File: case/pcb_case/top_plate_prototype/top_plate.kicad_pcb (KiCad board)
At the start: 2 copper layers, 143.4 x 111.8 mm, 7 parts

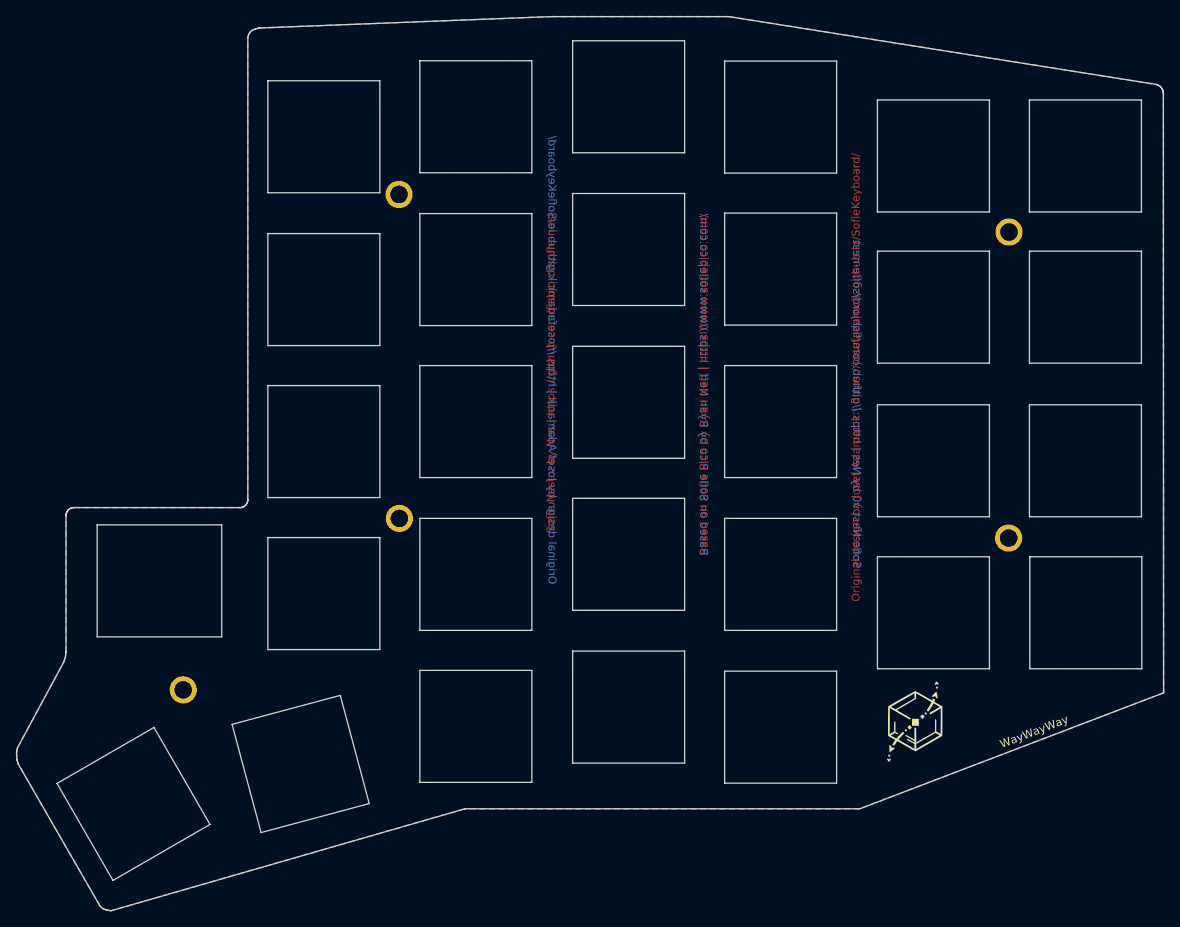
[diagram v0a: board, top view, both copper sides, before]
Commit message: Fix issues with case plates found during fabrication eval.
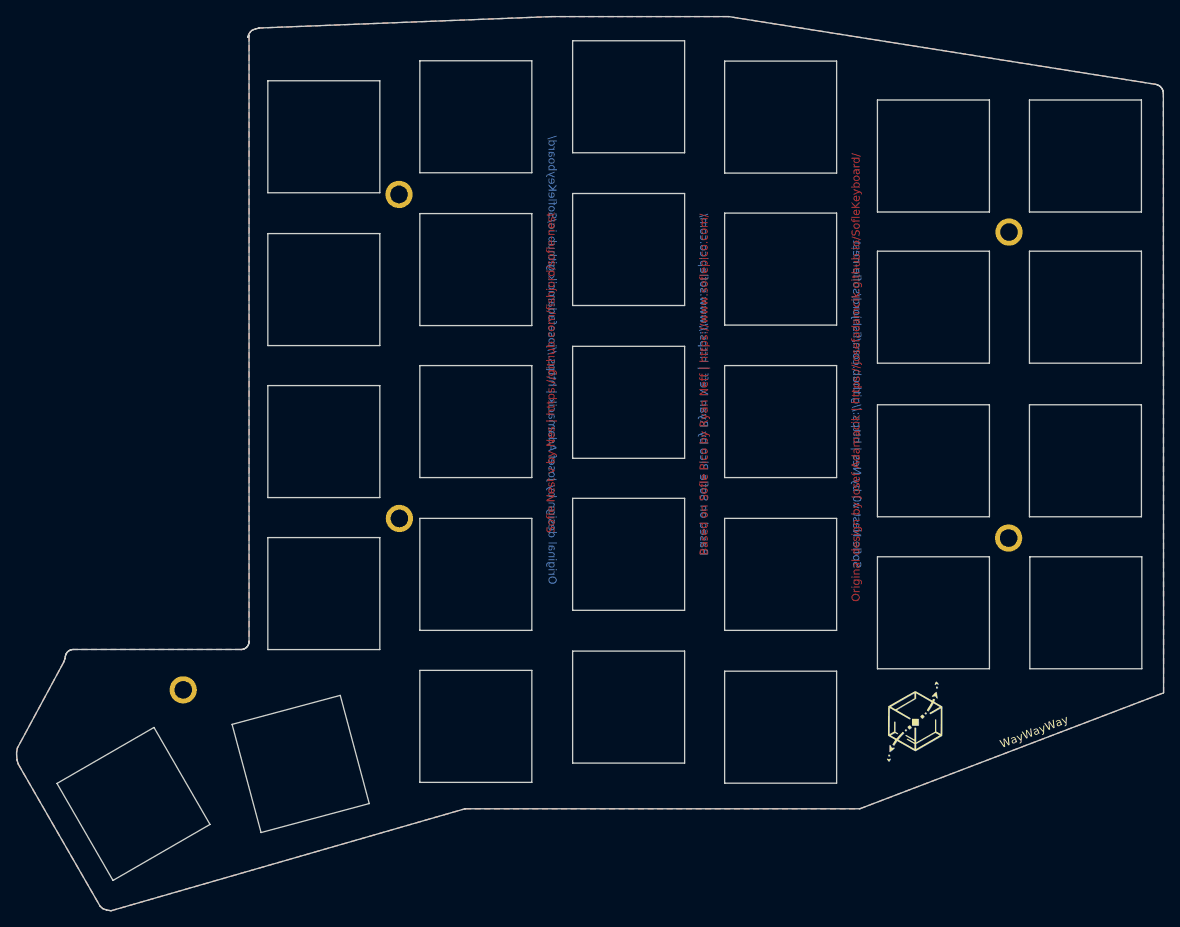
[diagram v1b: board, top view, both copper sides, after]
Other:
- outline, holes or cut-outs redrawn
